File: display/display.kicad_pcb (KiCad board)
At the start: 2 copper layers, 68.4 x 20.5 mm, 46 parts, among them P1 CONN_14

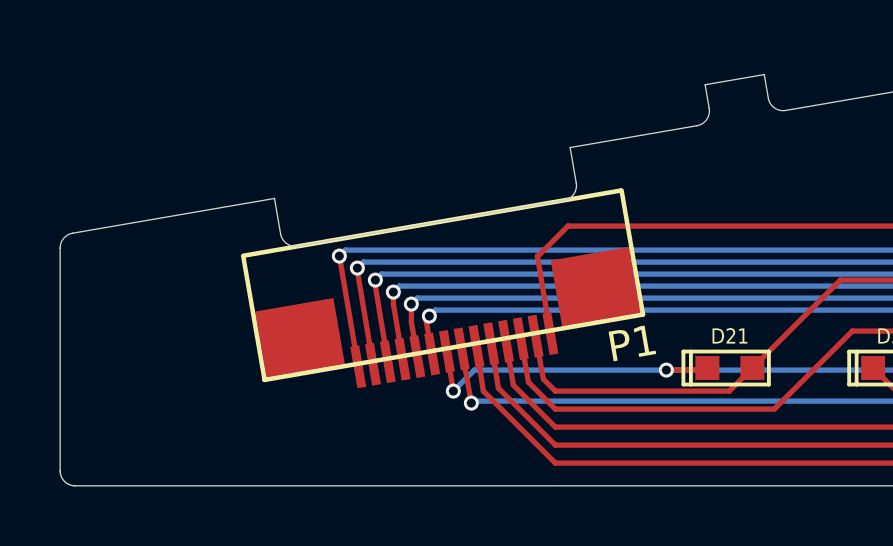
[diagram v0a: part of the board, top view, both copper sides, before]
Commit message: Replace FFC connectors with their 18 pin variant.
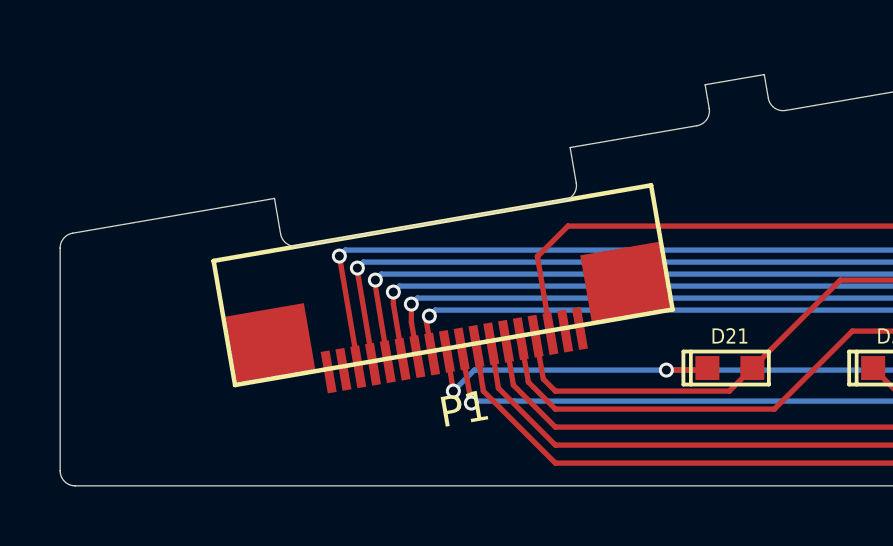
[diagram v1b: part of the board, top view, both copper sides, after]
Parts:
- P1: footprint SFV14R-2STE1HLF -> SFV18R-2STE1HLF
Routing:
- net /COL5: track 65.0 -> 115.0 mm, vias 4 -> 8
- net /COL1: track 27.0 -> 63.3 mm
- net /COL6: track 69.6 -> 34.3 mm, vias 4 -> 3
- net /ROW1: track 62.4 -> 32.3 mm
- net /COL7: track 73.1 -> 102.4 mm, vias 4 -> 6
- net /COL2: track 53.5 -> 80.2 mm
- net /ROW4: track 59.2 -> 34.4 mm
- net /COL8: track 69.6 -> 45.9 mm, vias 3 -> 0
- net /ROW3: track 64.2 -> 84.3 mm
- net /ROW5: track 62.5 -> 44.2 mm
- net /ROW6: track 44.9 -> 27.0 mm
- net /COL3: track 58.5 -> 45.1 mm, vias 4 -> 1
- net /COL4: track 72.8 -> 75.3 mm, vias 5 -> 6
- net /ROW2: track 59.8 -> 58.3 mm

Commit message: Update FFC connector module.
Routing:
- net /COL5: track 115.0 -> 68.0 mm, vias 8 -> 5
- net /COL3: track 45.1 -> 92.1 mm, vias 1 -> 4
- net /ROW1: track 32.3 -> 59.8 mm
- net /ROW3: track 84.3 -> 65.3 mm
- net /ROW4: track 34.4 -> 25.9 mm
- net /COL2: track 80.2 -> 80.9 mm, vias 4 -> 5
- net /COL4: track 75.3 -> 74.7 mm, vias 6 -> 5
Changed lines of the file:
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@@
   (general
     (links 90)
-    (no_connects 18)
+    (no_connects 15)
     (area 114.15 84.4 182.89528 109.763421)
     (thickness 1.6002)
@@
     (pad 18 smd rect (at 4.25 -4.3 189.8) (size 0.3 1.4)
       (layers Front F.Mask)
+      (clearance 0.1778)
     )
     (pad 17 smd rect (at 3.75 -4.3 189.8) (size 0.3 1.4)
       (layers Front F.Mask)
+      (clearance 0.1778)
     )
     (pad 1 smd rect (at -4.25 -4.3 189.8) (size 0.3 1.4)
       (layers Front F.Mask)
       (net 9 /ROW1)
+      (clearance 0.1778)
     )
     (pad 2 smd rect (at -3.75 -4.3 189.8) (size 0.3 1.4)
       (layers Front F.Mask)
       (net 10 /ROW2)
+      (clearance 0.1778)
     )
     (pad 6 smd rect (at -1.75 -4.3 189.8) (size 0.3 1.4)
       (layers Front F.Mask)
       (net 13 /ROW5)
+      (clearance 0.1778)
     )
     (pad 7 smd rect (at -1.25 -4.3 189.8) (size 0.3 1.4)
       (layers Front F.Mask)
       (net 8 /COL8)
+      (clearance 0.1778)
     )
     (pad 8 smd rect (at -0.75 -4.3 189.8) (size 0.3 1.4)
       (layers Front F.Mask)
       (net 1 /COL1)
+      (clearance 0.1778)
     )
     (pad 9 smd rect (at -0.25 -4.3 189.8) (size 0.3 1.4)
       (layers Front F.Mask)
       (net 7 /COL7)
+      (clearance 0.1778)
     )
     (pad 10 smd rect (at 0.25 -4.3 189.8) (size 0.3 1.4)
       (layers Front F.Mask)
       (net 6 /COL6)
+      (clearance 0.1778)
     )
     (pad 11 smd rect (at 0.75 -4.3 189.8) (size 0.3 1.4)
       (layers Front F.Mask)
       (net 2 /COL2)
+      (clearance 0.1778)
     )
     (pad 12 smd rect (at 1.25 -4.3 189.8) (size 0.3 1.4)
       (layers Front F.Mask)
       (net 3 /COL3)
+      (clearance 0.1778)
     )
     (pad 13 smd rect (at 1.75 -4.3 189.8) (size 0.3 1.4)
       (layers Front F.Mask)
       (net 4 /COL4)
+      (clearance 0.1778)
     )
     (pad 14 smd rect (at 2.25 -4.3 189.8) (size 0.3 1.4)
       (layers Front F.Mask)
       (net 5 /COL5)
+      (clearance 0.1778)
     )
     (pad 5 smd rect (at -2.25 -4.3 189.8) (size 0.3 1.4)
       (layers Front F.Mask)
       (net 12 /ROW4)
+      (clearance 0.1778)
     )
     (pad 15 smd rect (at 2.75 -4.3 189.8) (size 0.3 1.4)
       (layers Front F.Mask)
+      (clearance 0.1778)
     )
     (pad 16 smd rect (at 3.25 -4.3 189.8) (size 0.3 1.4)
       (layers Front F.Mask)
+      (clearance 0.1778)
     )
     (pad 4 smd rect (at -2.75 -4.3 189.8) (size 0.3 1.4)
       (layers Front F.Mask)
       (net 14 /ROW6)
+      (clearance 0.1778)
     )
     (pad 3 smd rect (at -3.25 -4.3 189.8) (size 0.3 1.4)
       (layers Front F.Mask)
       (net 11 /ROW3)
+      (clearance 0.1778)
     )
     (pad "" smd rect (at -6 -3.05 189.8) (size 2.65 2.3)
@@
   (via (at 126.8 104.1) (size 0.50038) (drill 0.29972) (layers Front Back) (net 2))
   (segment (start 126.7 104.3) (end 126.8 104.1) (width 0.1778) (layer Front) (net 2))
+  (segment (start 125.6 103.3) (end 125.8 103.1) (width 0.1778) (layer Back) (net 2))
+  (via (at 125.6 103.3) (size 0.50038) (drill 0.29972) (layers Front Back) (net 2))
+  (segment (start 125.6 103.7) (end 125.6 103.3) (width 0.1778) (layer Front) (net 2))
   (segment (start 157.34284 98.56978) (end 157.65526 98.56978) (width 0.1778) (layer Front) (net 3))
   (segment (start 157.65526 98.56978) (end 158.39186 97.83318) (width 0.1778) (layer Front) (net 3))
@@
   (segment (start 155.575 107.4801) (end 155.575 103.3907) (width 0.1778) (layer Back) (net 3))
   (segment (start 156.2862 108.1913) (end 155.575 107.4801) (width 0.1778) (layer Back) (net 3))
-  (segment (start 125.6 103.3) (end 125.8 103.1) (width 0.1778) (layer Back) (net 4))
-  (via (at 125.6 103.3) (size 0.50038) (drill 0.29972) (layers Front Back) (net 4))
-  (segment (start 125.6 103.7) (end 125.6 103.3) (width 0.1778) (layer Front) (net 4))
+  (via (at 158.39186 97.83318) (size 0.50038) (drill 0.29972) (layers Front Back) (net 3))
+  (via (at 163.99256 103.53294) (size 0.50038) (drill 0.29972) (layers Front Back) (net 3))
+  (segment (start 164.93998 100.73132) (end 165.19144 100.98278) (width 0.1778) (layer Front) (net 3))
+  (segment (start 165.19144 100.98278) (end 165.354 101.14534) (width 0.1778) (layer Front) (net 3))
+  (segment (start 150.9 102.7) (end 155.76682 97.83318) (width 0.1778) (layer Back) (net 3))
+  (segment (start 125.2 102.7) (end 150.9 102.7) (width 0.1778) (layer Back) (net 3))
+  (segment (start 155.76682 97.83318) (end 158.39186 97.83318) (width 0.1778) (layer Back) (net 3))
+  (segment (start 158.39186 97.83318) (end 161.54146 100.98278) (width 0.1778) (layer Back) (net 3))
+  (segment (start 161.54146 100.98278) (end 165.19144 100.98278) (width 0.1778) (layer Back) (net 3))
+  (segment (start 165.19144 102.33406) (end 165.19144 100.98278) (width 0.1778) (layer Back) (net 3))
+  (via (at 165.19144 100.98278) (size 0.50038) (drill 0.29972) (layers Front Back) (net 3))
+  (segment (start 163.99256 103.53294) (end 165.19144 102.33406) (width 0.1778) (layer Back) (net 3))
   (segment (start 125.907437 105.535121) (end 125.6 103.7) (width 0.1778) (layer Front) (net 4))
   (segment (start 124.4 102.5) (end 124.6 102.3) (width 0.1778) (layer Back) (net 4))
@@
   (via (at 125 102.9) (size 0.50038) (drill 0.29972) (layers Front Back) (net 5))
   (segment (start 125.414733 105.620225) (end 125 103.1) (width 0.1778) (layer Front) (net 5))
-  (segment (start 150.9 102.7) (end 155.76682 97.83318) (width 0.1778) (layer Back) (net 5))
-  (segment (start 125.2 102.7) (end 150.9 102.7) (width 0.1778) (layer Back) (net 5))
-  (segment (start 155.76682 97.83318) (end 158.39186 97.83318) (width 0.1778) (layer Back) (net 5))
-  (segment (start 158.39186 97.83318) (end 161.54146 100.98278) (width 0.1778) (layer Back) (net 5))
-  (via (at 158.39186 97.83318) (size 0.50038) (drill 0.29972) (layers Front Back) (net 5))
-  (segment (start 161.54146 100.98278) (end 165.19144 100.98278) (width 0.1778) (layer Back) (net 5))
-  (segment (start 165.19144 102.33406) (end 165.19144 100.98278) (width 0.1778) (layer Back) (net 5))
-  (via (at 165.19144 100.98278) (size 0.50038) (drill 0.29972) (layers Front Back) (net 5))
-  (segment (start 163.99256 103.53294) (end 165.19144 102.33406) (width 0.1778) (layer Back) (net 5))
-  (via (at 163.99256 103.53294) (size 0.50038) (drill 0.29972) (layers Front Back) (net 5))
-  (segment (start 164.93998 100.73132) (end 165.19144 100.98278) (width 0.1778) (layer Front) (net 5))
-  (segment (start 165.19144 100.98278) (end 165.354 101.14534) (width 0.1778) (layer Front) (net 5))
   (segment (start 124 101.9) (end 149.5 101.9) (width 0.1778) (layer Back) (net 5))
   (segment (start 124.429325 105.790435) (end 123.8 102.1) (width 0.1778) (layer Front) (net 5) (status 40000))
@@
   (segment (start 166.58082 95.58274) (end 165.58006 96.5835) (width 0.1778) (layer Front) (net 9))
   (segment (start 162.84194 98.56978) (end 160.84296 98.56978) (width 0.254) (layer Front) (net 9))
+  (segment (start 155 95.1) (end 149 101.1) (width 0.1778) (layer Front) (net 9))
+  (segment (start 131.419099 101.1) (end 130.402749 102.11635) (width 0.1778) (layer Front) (net 9))
+  (segment (start 131.419099 101.1) (end 149 101.1) (width 0.1778) (layer Front) (net 9))
+  (segment (start 130.402749 102.11635) (end 130.4 102.1) (width 0.1778) (layer Front) (net 9))
   (segment (start 159.7914 96.4914) (end 158.9 95.6) (width 0.1778) (layer Front) (net 10))
   (segment (start 159.7914 98.30308) (end 159.7914 96.4914) (width 0.1778) (layer Front) (net 10))
@@
   (segment (start 163.5633 99.33432) (end 160.1216 99.33432) (width 0.1778) (layer Front) (net 10))
   (segment (start 164.24402 98.6536) (end 163.5633 99.33432) (width 0.1778) (layer Front) (net 10))
-  (segment (start 131.419099 101.1) (end 130.402749 102.11635) (width 0.1778) (layer Front) (net 11))
-  (segment (start 131.419099 101.1) (end 149 101.1) (width 0.1778) (layer Front) (net 11))
-  (segment (start 155 95.1) (end 149 101.1) (width 0.1778) (layer Front) (net 11))
-  (segment (start 130.402749 102.11635) (end 130.4 102.1) (width 0.1778) (layer Front) (net 11))
   (segment (start 130.834477 104.684073) (end 130.402749 102.11635) (width 0.1778) (layer Front) (net 11))
   (segment (start 143.1 104.6) (end 140.9 104.6) (width 0.1778) (layer Front) (net 11))
@@
   (segment (start 156.35478 102.0826) (end 158.3309 102.0826) (width 0.1778) (layer Front) (net 11) (status 10))
   (segment (start 158.3309 102.0826) (end 159.38246 103.13416) (width 0.1778) (layer Front) (net 11))
-  (segment (start 130.1 106.3) (end 131 107.2) (width 0.1778) (layer Front) (net 12))
+  (segment (start 131 107.2) (end 138.3 107.2) (width 0.1778) (layer Front) (net 11))
+  (segment (start 130.1 106.3) (end 131 107.2) (width 0.1778) (layer Front) (net 11))
   (segment (start 130.1 106.3) (end 129.849069 104.854283) (width 0.1778) (layer Front) (net 12))
-  (segment (start 131 107.2) (end 138.3 107.2) (width 0.1778) (layer Front) (net 12))
   (segment (start 173.24324 105.5116) (end 172.56506 104.83342) (width 0.1778) (layer Front) (net 12))
   (segment (start 173.24324 105.5116) (end 173.98746 105.5116) (width 0.1778) (layer Front) (net 12))

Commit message: Move the boards away from nearby texts because this way it's easier to wrap a ground fill around the boards without the text visually interfering.
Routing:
- net /COL5: track 68.0 -> 67.5 mm, vias 5 -> 4
- net /COL3: track 92.1 -> 92.6 mm, vias 4 -> 5
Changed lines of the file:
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@@
     (effects (font (size 1.016 0.762) (thickness 0.1524)) (justify left mirror))
   )
-  (gr_text "* 1.55mm board thickness\n* black soldermask\n* white silkscreen\n" (at 114.3 85.9) (layer Cmts.User)
+  (gr_text "* 1.55mm board thickness\n* black soldermask\n* white silkscreen\n" (at 114 73) (layer Cmts.User)
     (effects (font (size 1.5 1.5) (thickness 0.3)) (justify left))
   )
@@
   (via (at 165.19144 100.98278) (size 0.50038) (drill 0.29972) (layers Front Back) (net 3))
   (segment (start 163.99256 103.53294) (end 165.19144 102.33406) (width 0.1778) (layer Back) (net 3))
+  (segment (start 125 102.9) (end 125.2 102.7) (width 0.1778) (layer Back) (net 3))
+  (via (at 125 102.9) (size 0.50038) (drill 0.29972) (layers Front Back) (net 3))
+  (segment (start 125 103.1) (end 125 102.9) (width 0.1778) (layer Front) (net 3))
   (segment (start 125.907437 105.535121) (end 125.6 103.7) (width 0.1778) (layer Front) (net 4))
   (segment (start 124.4 102.5) (end 124.6 102.3) (width 0.1778) (layer Back) (net 4))
@@
   (segment (start 167.10406 106.55808) (end 167.11676 106.55808) (width 0.1778) (layer Front) (net 4))
   (segment (start 167.11676 106.55808) (end 167.10406 106.55808) (width 0.1778) (layer Front) (net 4))
-  (segment (start 125 102.9) (end 125.2 102.7) (width 0.1778) (layer Back) (net 5))
-  (segment (start 125 103.1) (end 125 102.9) (width 0.1778) (layer Front) (net 5))
-  (via (at 125 102.9) (size 0.50038) (drill 0.29972) (layers Front Back) (net 5))
   (segment (start 125.414733 105.620225) (end 125 103.1) (width 0.1778) (layer Front) (net 5))
   (segment (start 124 101.9) (end 149.5 101.9) (width 0.1778) (layer Back) (net 5))

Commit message: Update schematic to use the 18 pin connector.  Update netlist.
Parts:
- P1: value CONN_14 -> CONN_18
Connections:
- P1 pad 1: /ROW1 -> GND
- P1 pad 10: /COL6 -> GND
- P1 pad 11: /COL2 -> /COL1
- P1 pad 12: /COL3 -> /COL7
- P1 pad 13: /COL4 -> /COL6
- P1 pad 14: /COL5 -> /COL2
- P1 pad 15: (no net) -> /COL3
- P1 pad 16: (no net) -> /COL4
- P1 pad 17: (no net) -> /COL5
- P1 pad 18: (no net) -> GND
- P1 pad 2: /ROW2 -> /ROW1
- P1 pad 3: /ROW3 -> /ROW2
- P1 pad 4: /ROW6 -> /ROW3
- P1 pad 5: /ROW4 -> /ROW6
- P1 pad 6: /ROW5 -> /ROW4
- P1 pad 7: /COL8 -> /ROW5
- P1 pad 8: /COL1 -> /COL8
- P1 pad 9: /COL7 -> GND
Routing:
- net GND: track 0.00 -> 59.9 mm, vias 0 -> 3
- net /COL5: track 67.5 -> 35.4 mm, vias 4 -> 3
- net /COL2: track 80.9 -> 54.2 mm, vias 5 -> 4
- net /COL7: track 102.4 -> 80.5 mm, vias 6 -> 4
- net /ROW4: track 25.9 -> 43.7 mm
- net /ROW5: track 44.2 -> 59.8 mm
- net /COL4: track 74.7 -> 66.0 mm
- net /COL1: track 63.3 -> 55.0 mm, vias 3 -> 4
- net /COL8: track 45.9 -> 48.7 mm
- net /ROW2: track 58.3 -> 60.9 mm
- net /ROW3: track 65.3 -> 64.2 mm
- net /COL6: track 34.3 -> 34.8 mm

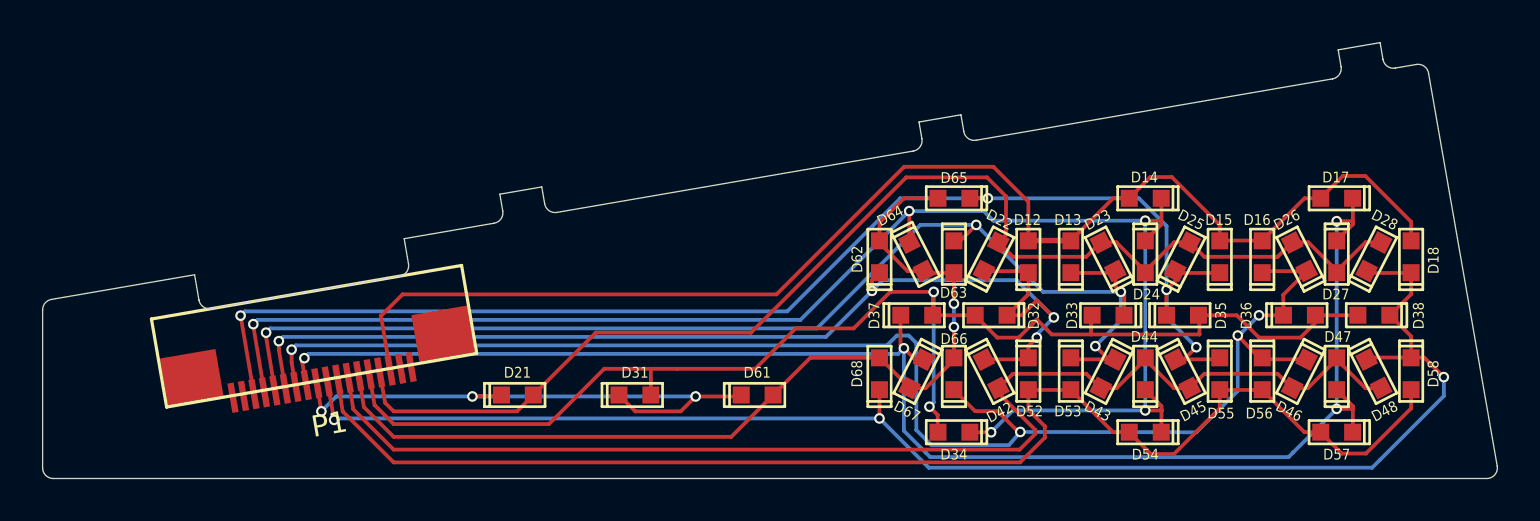
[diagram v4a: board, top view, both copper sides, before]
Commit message: Update PCB outline and FFC connector position.
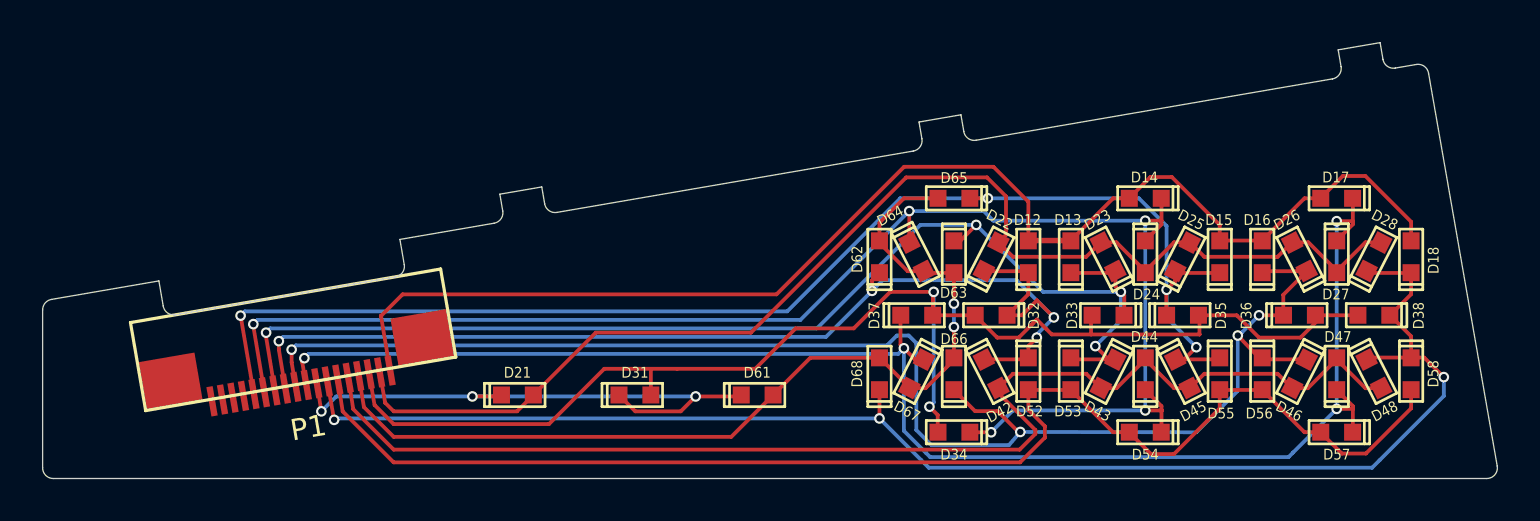
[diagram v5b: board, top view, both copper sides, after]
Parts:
- moved P1 1.00 mm to (125.9, 101.2)
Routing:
- net /COL3: track 92.2 -> 20.2 mm, vias 5 -> 3
- net /ROW4: track 43.7 -> 95.4 mm
- net /COL6: track 34.8 -> 75.4 mm, vias 3 -> 4
- net /ROW5: track 59.8 -> 26.7 mm
- net /COL4: track 66.0 -> 36.5 mm, vias 5 -> 4
- net /COL1: track 55.0 -> 27.5 mm, vias 4 -> 3
- net /COL2: track 54.2 -> 81.1 mm, vias 4 -> 5
- net /COL8: track 48.7 -> 69.1 mm, vias 0 -> 3
- net /ROW3: track 64.2 -> 82.1 mm
- net GND: track 59.9 -> 62.4 mm, vias 3 -> 2
- net /COL7: track 80.5 -> 82.0 mm
- net /ROW1: track 59.8 -> 61.3 mm
- net /ROW2: track 60.9 -> 59.8 mm
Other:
- outline, holes or cut-outs redrawn

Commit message: Connect every net.
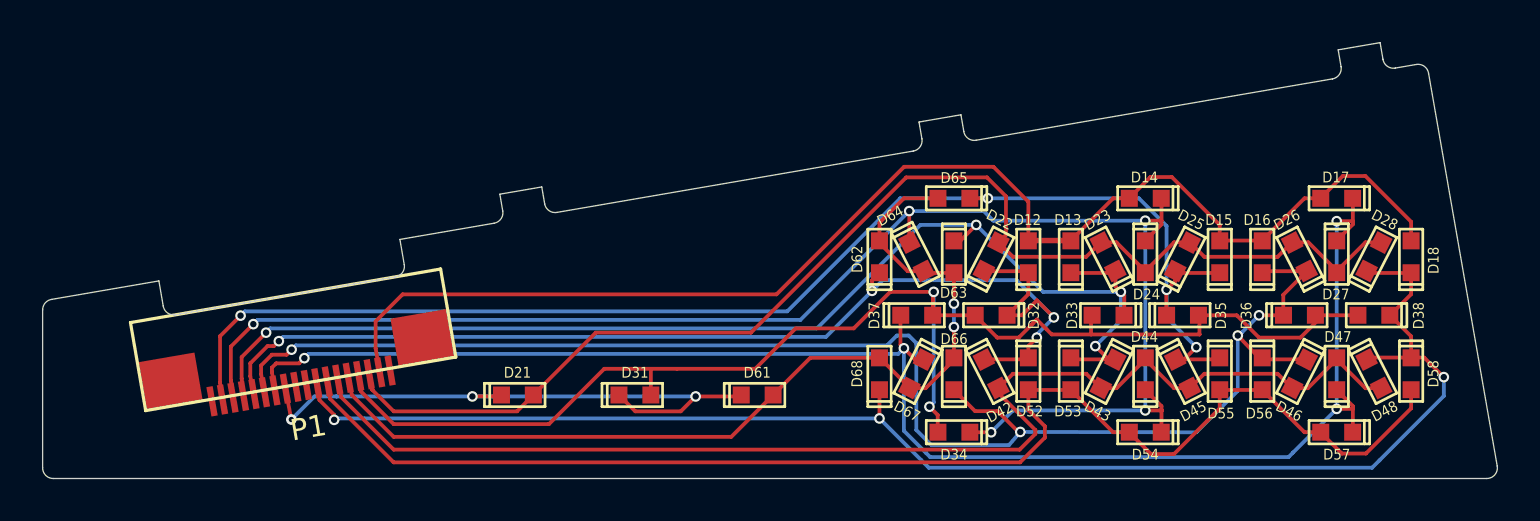
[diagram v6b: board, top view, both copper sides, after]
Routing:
- net GND: track 62.4 -> 0.00 mm, vias 2 -> 0
- net /COL3: track 20.2 -> 59.2 mm, vias 3 -> 4
- net /COL4: track 36.5 -> 73.4 mm, vias 4 -> 5
- net /ROW4: track 95.4 -> 59.4 mm
- net /ROW5: track 26.7 -> 62.7 mm
- net /COL5: track 35.4 -> 65.6 mm, vias 3 -> 4
- net /COL2: track 81.1 -> 54.4 mm, vias 5 -> 4
- net /ROW6: track 27.0 -> 45.0 mm
- net /ROW3: track 82.1 -> 64.4 mm
- net /COL7: track 82.0 -> 74.6 mm
- net /COL6: track 75.4 -> 70.9 mm
- net /ROW1: track 61.3 -> 62.6 mm
- net /COL1: track 27.5 -> 28.7 mm
- net /COL8: track 69.1 -> 69.8 mm
